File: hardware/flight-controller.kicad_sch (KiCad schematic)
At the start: 10 parts, among them J1 Conn_01x03, J2 Conn_01x03, J3 Conn_01x03, J4 Conn_01x03, J5 Conn_01x02, J6 Conn_01x02, J7 Conn_01x02, J8 Conn_01x02, U1 STM32H723VGTx, U2 LSM6DSOTR

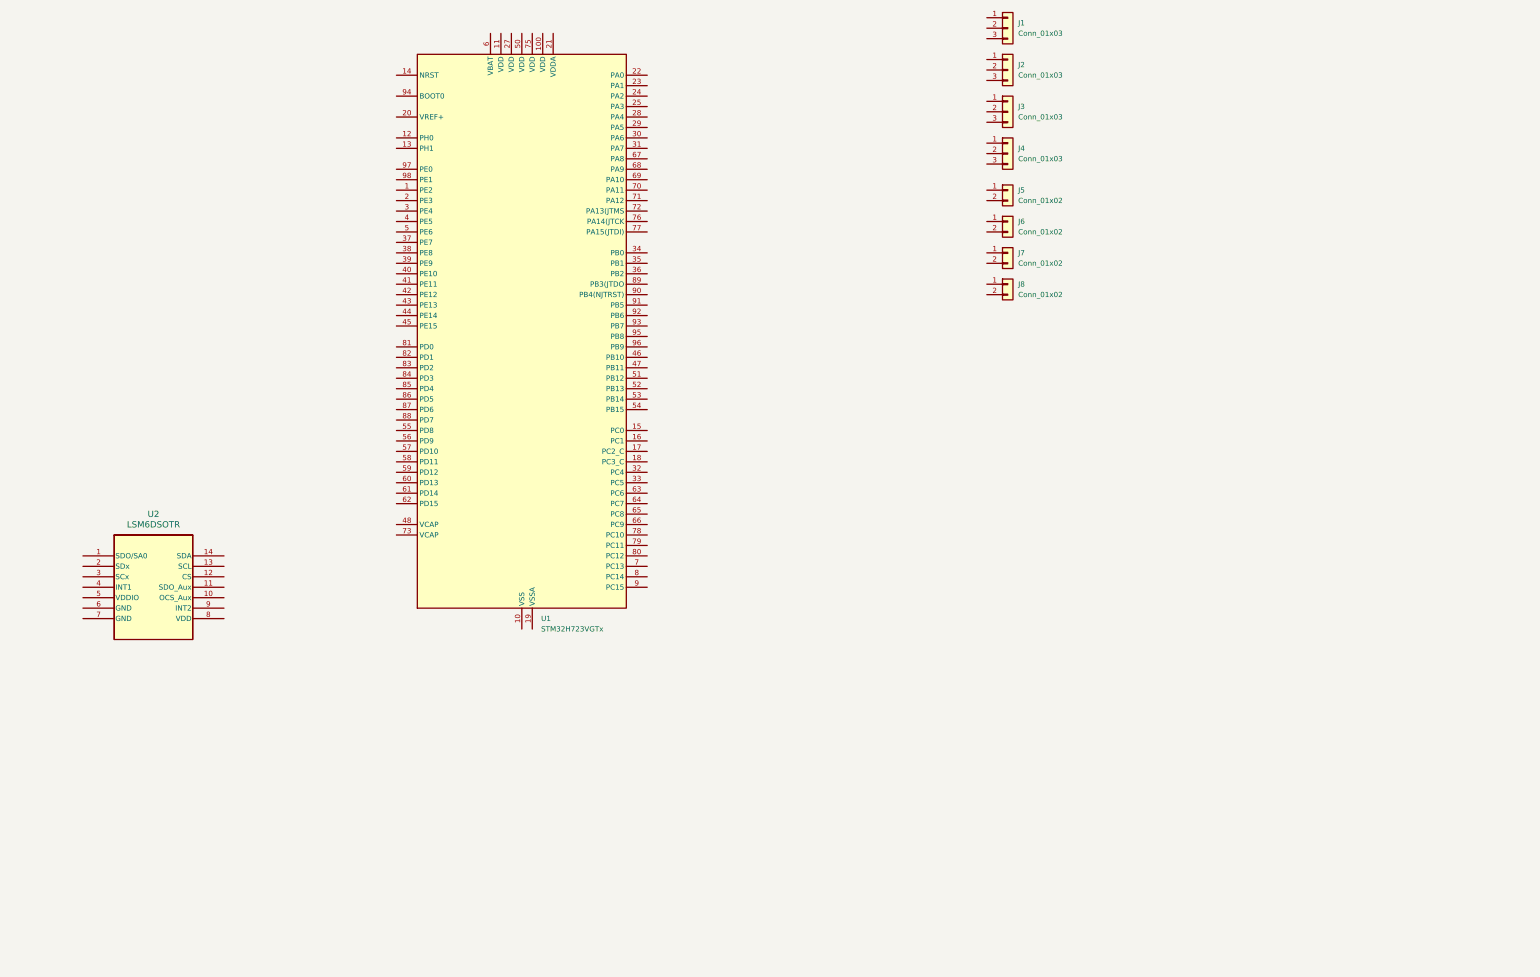
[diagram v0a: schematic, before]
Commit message: made schematic outline
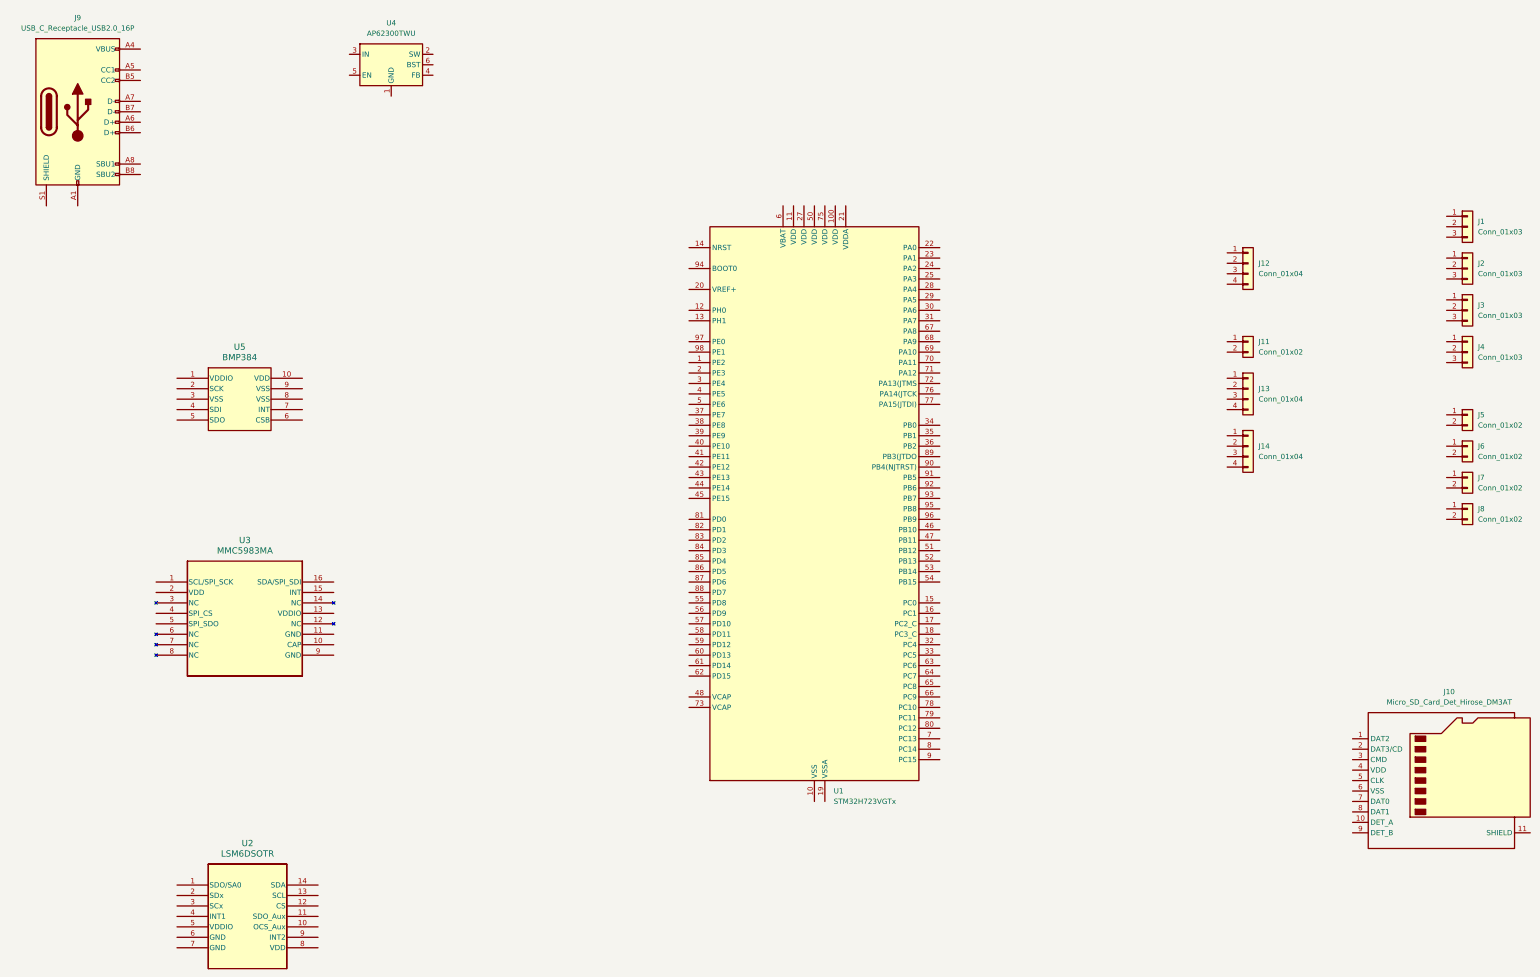
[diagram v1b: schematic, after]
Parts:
- removed U2: LSM6DSOTR, LGA-14L_2P5X3X0P86_STM, symbol Imports:LSM6DSOTR
- added J10: Micro_SD_Card_Det_Hirose_DM3AT, symbol Connector:Micro_SD_Card_Det_Hirose_DM3AT
- added J11: Conn_01x02, symbol Connector_Generic:Conn_01x02
- added J12, J13, J14: Conn_01x04, symbol Connector_Generic:Conn_01x04
- added J9: USB_C_Receptacle_USB2.0_16P, symbol Connector:USB_C_Receptacle_USB2.0_16P
- added U2: LSM6DSOTR, LGA-14L_2P5X3X0P86_STM, symbol Flight-Controller_Imports:LSM6DSOTR
- added U3: MMC5983MA, MMC5983MA_MEM, symbol Flight-Controller_Imports:MMC5983MA
- added U4: AP62300TWU, Package_TO_SOT_SMD:TSOT-23-6, symbol Regulator_Switching:AP62300TWU
- added U5: BMP384, LGA10_2.0X2.0X0.95_BOS, symbol Flight-Controller_Imports:BMP384
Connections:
- new net: J9.A1 (GND), J9.A12 (GND), J9.B1 (GND), J9.B12 (GND)
- new net: J9.A4 (VBUS), J9.A9 (VBUS), J9.B4 (VBUS), J9.B9 (VBUS)
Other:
- moved on the sheet: J1, J2, J3, J4, J5, J6, J7, J8, U1
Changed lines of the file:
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@@
 	(generator "eeschema")
 	(generator_version "9.0")
-	(paper "A4")
+	(paper "A3")

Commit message: added gps
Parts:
- added U6: NEO-M9N, RF_GPS:ublox_NEO, symbol RF_GPS:NEO-M9N
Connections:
- new net: U6.10 (GND), U6.12 (GND), U6.13 (GND), U6.24 (GND)
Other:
- moved on the sheet: J1, J11, J12, J13, J14, J2, J3, J4, J5, J6, J7, J8

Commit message: worked on schematic
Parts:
- added BOOT, RESET: SW_Push, symbol Switch:SW_Push
- added C1, C17, C2, C21, C23, C24, C27, C3, C4, C5, C8, C9: 100nF, Capacitor_SMD:C_0402_1005Metric, symbol Device:C
- added C10: 4.7uF, Capacitor_SMD:C_0402_1005Metric, symbol Device:C
- added C11, C12: 2.2uF, Capacitor_SMD:C_0402_1005Metric, symbol Device:C
- added C13, C14: 27pF, Capacitor_SMD:C_0402_1005Metric, symbol Device:C
- added C15, C16: 15pF, Capacitor_SMD:C_0402_1005Metric, symbol Device:C
- added C18, C25: 10uF, Capacitor_SMD:C_0402_1005Metric, symbol Device:C
- added C19, C20: 22uF, Capacitor_SMD:C_0402_1005Metric, symbol Device:C
- added C22: 10pF, Capacitor_SMD:C_0402_1005Metric, symbol Device:C
- added C26, C6, C7: 1uF, Capacitor_SMD:C_0402_1005Metric, symbol Device:C
- added D1: LED, LED_SMD:LED_0603_1608Metric, symbol Device:LED
- added FB1: FerriteBead, symbol Device:FerriteBead
- added L1: 3.3uH, symbol Device:L
- added R1: 47, symbol Device:R
- added R10, R11, R12, R13, R14, R15, R2, R3, R8: 10K, symbol Device:R
- added R4, R5: 27, symbol Device:R
- added R6, R7: 5.1K, symbol Device:R
- added R9: 33.2K, symbol Device:R
- added Y1: Q13FC13500004, symbol Device:Crystal
- added Y2: X322512MSB4SI, symbol Device:Crystal_GND24
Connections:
- net GND: now reaches U1.10 (VSS), U1.26 (VSS), U1.49 (VSS), U1.74 (VSS), U1.99 (VSS)
- net GND: now also J10.11 (SHIELD), J10.6 (VSS), J9.A1 (GND), J9.A12 (GND), J9.B1 (GND), J9.B12 (GND), J9.S1 (SHIELD), U1.19 (VSSA), U2.2 (SDx), U2.3 (SCx), U2.6 (GND), U2.7 (GND), U3.11 (GND), U3.9 (GND), U4.1 (GND), C1.2, C10.2, C11.2, C12.2, C13.2, C14.2, C15.2, C16.2, C17.1, C18.2, C19.2, C2.2, C20.2, C23.2, C24.2, C25.2, C26.2, C27.2, C3.2, C4.2, C5.2, C6.2, C7.2, C8.2, C9.2, D1.1 (K), R2.2, R6.2, R7.1, R9.2, RESET.1, Y2.2 (G), Y2.4 (G)
- net +3.3V: now reaches U1.100 (VDD)
- net +3.3V: now also J10.4 (VDD), U1.11 (VDD), U1.27 (VDD), U1.50 (VDD), U1.6 (VBAT), U1.75 (VDD), U2.5 (VDDIO), U2.8 (VDD), U3.13 (VDDIO), U3.2 (VDD), U3.4 (SPI_CS), BOOT.1, C1.1, C10.1, C19.1, C2.1, C20.1, C22.1, C23.1, C24.1, C26.1, C27.1, C3.1, C4.1, C5.1, C6.1, C7.1, C8.1, C9.1, FB1.1, L1.2, R1.1, R10.1, R11.1, R12.1, R13.1, R14.1, R15.1, R8.1
- net HSE_IN: now reaches U1.12 (PH0)
- net HSE_IN: now also C13.1, Y2.1
- net HSE_OUT: now reaches U1.13 (PH1)
- net HSE_OUT: now also C14.1, Y2.3
- net RESET: now reaches U1.14 (NRST)
- net RESET: now also C17.2, RESET.2
- net at U1.20 (VREF+): now also R1.2
- net at U1.21 (VDDA): now also FB1.2
- net UART4_TX: now reaches U1.22 (PA0)
- net UART4_RX: now reaches U1.23 (PA1)
- net UART2_TX: now reaches U1.24 (PA2)
- net UART2_RX: now reaches U1.25 (PA3)
- net SPI_NSS: now reaches U1.28 (PA4)
- net SPI_NSS: now also U2.12 (CS)
- net SPI_SCK: now reaches U1.29 (PA5)
- net SPI_SCK: now also U2.13 (SCL)
- net SPI_MISO: now reaches U1.30 (PA6)
- net SPI_MISO: now also U2.1 (SDO/SA0)
- net SPI_MOSI: now reaches U1.31 (PA7)
- net SPI_MOSI: now also U2.14 (SDA)
- net LSM_INT: now reaches U1.32 (PC4)
- net LSM_INT: now also U2.4 (INT1)
- net BAT_ADC: now reaches U1.34 (PB0)
- net UART3_TX: now reaches U1.46 (PB10)
- net UART3_RX: now reaches U1.47 (PB11)
- net at U1.48 (VCAP): now also C12.1
- net GPS_INT: now reaches U1.52 (PB13)
- net GPS_TX: now reaches U1.53 (PB14)
- net GPS_RX: now reaches U1.54 (PB15)
- net PWM_1: now reaches U1.59 (PD12)
- net PWM_2: now reaches U1.60 (PD13)
- net PWM_3: now reaches U1.61 (PD14)
- net PWM_4: now reaches U1.62 (PD15)
- net SD_D0: now reaches U1.65 (PC8)
- net SD_D0: now also J10.7 (DAT0), R11.2
- net SD_D1: now reaches U1.66 (PC9)
- net SD_D1: now also J10.8 (DAT1), R10.2
- net at U1.70 (PA11): now also R4.1
- net at U1.71 (PA12): now also R5.2
- net SWDIO: now reaches U1.72 (PA13(JTMS)
- net at U1.73 (VCAP): now also C11.1
- net SWDCLK: now reaches U1.76 (PA14(JTCK)
- net SD_D2: now reaches U1.78 (PC10)
- net SD_D2: now also J10.1 (DAT2), R15.2
- net SD_D3: now reaches U1.79 (PC11)
- net SD_D3: now also J10.2 (DAT3/CD), R14.2
- net LSE_IN: now reaches U1.8 (PC14)
- net LSE_IN: now also C15.1, Y1.1
- net SD_CLK: now reaches U1.80 (PC12)
- net SD_CLK: now also J10.5 (CLK), R12.2
- net SD_CMD: now reaches U1.83 (PD2)
- net SD_CMD: now also J10.3 (CMD), R13.2
- net SD_DET1: now reaches U1.84 (PD3)
- net SD_DET1: now also J10.10 (DET_A)
- net SD_DET2: now reaches U1.85 (PD4)
- net SD_DET2: now also J10.9 (DET_B)
- net LSE_OUT: now reaches U1.9 (PC15)
- net LSE_OUT: now also C16.1, Y1.2
- net BMP_INT: now reaches U1.90 (PB4(NJTRST))
- net MMC_INT: now reaches U1.91 (PB5)
- net MMC_INT: now also U3.15 (INT)
- net SCL: now reaches U1.92 (PB6)
- net SCL: now also U3.1 (SCL/SPI_SCK)
- net SDA: now reaches U1.93 (PB7)
- net SDA: now also U3.16 (SDA/SPI_SDI)
- net BOOT: now reaches U1.94 (BOOT0)
- net BOOT: now also BOOT.2, R2.1
- net at U1.97 (PE0): now also R3.1
- net at U3.10 (CAP): now also C25.1
- net VBUS: now reaches J9.A4 (VBUS), J9.A9 (VBUS), J9.B4 (VBUS), J9.B9 (VBUS)
- net VBUS: now also U4.3 (IN), U4.5 (EN), C18.1
- net at J9.A5 (CC1): now also R6.1
- net USB_-: now reaches J9.A6 (D+)
- net USB_-: now also J9.B6 (D+), R4.2
- net USB_+: now reaches J9.A7 (D-)
- net USB_+: now also J9.B7 (D-), R5.1
- net at J9.B5 (CC2): now also R7.2
- net at U4.2 (SW): now also C21.1, L1.1
- net at U4.4 (FB): now also C22.2, R8.2, R9.1
- net at U4.6 (BST): now also C21.2
- new net: D1.2 (A), R3.2
- no-connect marks 0 -> 6
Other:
- moved on the sheet: J10, J9, U1, U2, U3, U4, U5

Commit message: routed schematic
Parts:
- removed J12: Conn_01x04, symbol Connector_Generic:Conn_01x04
- added BT1: Battery, symbol Device:Battery_Cell
- added C28, C29: 100nF, Capacitor_SMD:C_0402_1005Metric, symbol Device:C
- added C30, C35: 1uF, Capacitor_SMD:C_0402_1005Metric, symbol Device:C
- added C31, C32, C33, C34, C36, C37: 10uF, Capacitor_SMD:C_0402_1005Metric, symbol Device:C
- added D2, D3: LED, LED_SMD:LED_0603_1608Metric, symbol Device:LED
- added D4: D_Schottky, symbol Device:D_Schottky
- added J12, J16: Conn_01x02, symbol Connector_Generic:Conn_01x02
- added J15: Conn_Coaxial, Connector_Coaxial:U.FL_Molex_MCRF_73412-0110_Vertical, symbol Connector:Conn_Coaxial
- added J17: Conn_01x04, symbol Connector_Generic:Conn_01x04
- added R16, R17, R18: 1K, symbol Device:R
- added R19: 3K, symbol Device:R
- added R20, R22, R24, R26: 5K, symbol Device:R
- added R21: 23.7, symbol Device:R
- added R23: 60K, symbol Device:R
- added R25, R27: 30K, symbol Device:R
- added TP1: TestPoint, Connector_Pin:Pin_D1.0mm_L10.0mm_LooseFit, symbol Connector:TestPoint
- added U7: TPS2121RUXR, TPS2121RUXR:IC_TPS2121RUXR, symbol Flight-Controller_Imports:TPS2121RUXR
- R3: value 10K -> 1K
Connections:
- net +3.3V: now also J13.1 (Pin_1), J14.1 (Pin_1), U5.1 (VDDIO), U5.10 (VDD), U6.23 (VCC), C28.1, C29.1, C37.1, D4.2 (A), J12.1 (Pin_1), J17.1 (Pin_1), R17.1
- net BMP_INT: now also U5.7 (INT)
- net GND: now also J1.3 (Pin_3), J11.2 (Pin_2), J13.2 (Pin_2), J14.2 (Pin_2), J2.3 (Pin_3), J3.3 (Pin_3), J4.3 (Pin_3), J5.2 (Pin_2), J6.2 (Pin_2), J7.2 (Pin_2), J8.2 (Pin_2), U5.3 (VSS), U5.5 (SDO), U5.8 (VSS), U5.9 (VSS), U6.10 (GND), U6.12 (GND), U6.13 (GND), U6.24 (GND), U6.7 (VDD_USB), BT1.2 (-), C28.2, C29.2, C30.2, C31.2, C32.2, C33.2, C34.2, C35.2, C36.2, C37.2, D2.1 (K), D3.1 (K), J12.2 (Pin_2), J15.2 (Ext), J16.2 (Pin_2), J17.2 (Pin_2), R20.2, R22.2, R24.2, R26.2, R27.2, U7.12 (GND), U7.9 (ST)
- net GPS_INT: now also U6.4 (EXTINT)
- net GPS_RX: now also U6.20 (TXD/SPI_MISO)
- net GPS_TX: now also U6.21 (RXD/SPI_MOSI)
- net PWM_1: now also J1.1 (Pin_1)
- net PWM_2: now also J2.1 (Pin_1)
- net PWM_3: now also J3.1 (Pin_1)
- net PWM_4: now also J4.1 (Pin_1)
- net SCL: now also U5.2 (SCK)
- net SDA: now also U5.4 (SDI)
- net UART2_RX: now also J13.4 (Pin_4)
- net UART2_TX: now also J13.3 (Pin_3)
- net UART3_RX: now also J17.4 (Pin_4)
- net UART3_TX: now also J17.3 (Pin_3)
- net UART4_RX: now also J14.4 (Pin_4)
- net UART4_TX: now also J14.3 (Pin_3)
- net VBUS: now also R19.1, R21.1, U7.7 (IN1); no longer C18.1, U4.3 (IN), U4.5 (EN)
- net LSM_INT2: now reaches U1.33 (PC5)
- net LSM_INT2: now also U2.9 (INT2)
- net GPS_RESET: now reaches U1.51 (PB12)
- net GPS_RESET: now also U6.8 (~{RESET})
- net STAT_LED: now reaches R3.1, U1.97 (PE0)
- net +BATT: now reaches J11.1 (Pin_1)
- net +BATT: now also J5.1 (Pin_1), J6.1 (Pin_1), J7.1 (Pin_1), J8.1 (Pin_1), C31.1, C32.1, C33.1, C34.1, C36.1, J16.1 (Pin_1), R23.1, R25.1, U7.2 (IN2)
- net at U6.1 (~{SAFEBOOT}): now also TP1.1
- net at U6.11 (RF_IN): now also J15.1 (In)
- net V_BCKP: now reaches U6.22 (V_BCKP)
- net V_BCKP: now also BT1.1 (+), C30.1, R18.2
- net GPS_LED: now reaches U6.3 (TIMEPULSE)
- net GPS_LED: now also R16.1
- net LSM_INT renamed LSM_INT1
- new net: R23.2, R24.1, U7.4 (OV2)
- new net: D2.2 (A), R16.2
- new net: R21.2, R22.1, U7.5 (OV1)
- new net: R25.2, R26.1, U7.3 (CP2)
- new net: R27.1, U7.10 (ILIM)
- new net: C35.1, U7.11 (SS)
- new net: R19.2, R20.1, U7.6 (PR1)
- new net: D4.1 (K), R18.1
- new net: D3.2 (A), R17.2
- new net VDD: C18.1, U4.3 (IN), U4.5 (EN), U7.1 (OUT), U7.8 (OUT__2)
- no-connect marks 6 -> 17
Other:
- moved on the sheet: BOOT, C1, C10, C11, C12, C13, C14, C15, C16, C17, C18, C19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

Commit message: worked on layout
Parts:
- removed J11, J12, J5, J6, J7, J8: Conn_01x02, symbol Connector_Generic:Conn_01x02
- added C38: 22uF, Capacitor_SMD:C_1206_3216Metric, symbol Device:C
- added J10, J16, J18, J5, J7, J9: Screw_Terminal_01x02, TerminalBlock_4Ucon:TerminalBlock_4Ucon_1x02_P3.50mm_Horizontal, symbol Connector:Screw_Terminal_01x02
- BOOT1: renamed from BOOT; footprint (none) -> Button_Switch_SMD:SW_Push_SPST_NO_Alps_SKRK
- BT1: value Battery -> MS621FE-FL11E; footprint (none) -> Flight-Controller_Imports:BAT_MS621FE-FL11E
- C1: renamed from C26; footprint Capacitor_SMD:C_0402_1005Metric -> Capacitor_SMD:C_0603_1608Metric
- C14: value 27pF -> 18pF
- C16: renamed from C18; footprint Capacitor_SMD:C_0402_1005Metric -> Capacitor_SMD:C_0603_1608Metric
- C19: renamed from C6; footprint Capacitor_SMD:C_0402_1005Metric -> Capacitor_SMD:C_0603_1608Metric
- C21: renamed from C7; footprint Capacitor_SMD:C_0402_1005Metric -> Capacitor_SMD:C_0603_1608Metric
- C26: renamed from C19; footprint Capacitor_SMD:C_0402_1005Metric -> Capacitor_SMD:C_0603_1608Metric
- C28: renamed from C20; footprint Capacitor_SMD:C_0402_1005Metric -> Capacitor_SMD:C_0603_1608Metric
- C31: renamed from C10; footprint Capacitor_SMD:C_0402_1005Metric -> Capacitor_SMD:C_0603_1608Metric
- C32: renamed from C36; footprint Capacitor_SMD:C_0402_1005Metric -> Capacitor_SMD:C_0805_2012Metric
- C33: renamed from C37; footprint Capacitor_SMD:C_0402_1005Metric -> Capacitor_SMD:C_0805_2012Metric
- C34: renamed from C31; footprint Capacitor_SMD:C_0402_1005Metric -> Capacitor_SMD:C_0805_2012Metric
- C35: renamed from C33; footprint Capacitor_SMD:C_0402_1005Metric -> Capacitor_SMD:C_0805_2012Metric
- C36: renamed from C32; footprint Capacitor_SMD:C_0402_1005Metric -> Capacitor_SMD:C_0805_2012Metric
- C37: renamed from C34; footprint Capacitor_SMD:C_0402_1005Metric -> Capacitor_SMD:C_0805_2012Metric
- C5: renamed from C25; footprint Capacitor_SMD:C_0402_1005Metric -> Capacitor_SMD:C_0603_1608Metric
- C8: renamed from C30; footprint Capacitor_SMD:C_0402_1005Metric -> Capacitor_SMD:C_0603_1608Metric
- C9: renamed from C13; value 27pF -> 18pF
- D1: renamed from D4; footprint (none) -> Diode_SMD:D_0603_1608Metric
- FB1: footprint (none) -> Inductor_SMD:L_0603_1608Metric
- J1: renamed from J9; footprint (none) -> Connector_USB:USB_C_Receptacle_GCT_USB4105-xx-A_16P_TopMnt_Horizontal
- J11: renamed from J10; footprint (none) -> Connector_Card:microSD_HC_Hirose_DM3AT-SF-PEJM5
- J12: renamed from J1; footprint (none) -> Connector_PinHeader_2.54mm:PinHeader_1x03_P2.54mm_Vertical
- J13: renamed from J2; footprint (none) -> Connector_PinHeader_2.54mm:PinHeader_1x03_P2.54mm_Vertical
- J14: renamed from J3; footprint (none) -> Connector_PinHeader_2.54mm:PinHeader_1x03_P2.54mm_Vertical
- J15: renamed from J4; footprint (none) -> Connector_PinHeader_2.54mm:PinHeader_1x03_P2.54mm_Vertical
- J2: renamed from J16; footprint (none) -> Connector_AMASS:AMASS_XT60-M_1x02_P7.20mm_Vertical
- J4: renamed from J13; footprint (none) -> Connector_JST:JST_XH_B4B-XH-A_1x04_P2.50mm_Vertical
- J6: renamed from J17; footprint (none) -> Connector_JST:JST_XH_B4B-XH-A_1x04_P2.50mm_Vertical
- J8: renamed from J14; footprint (none) -> Connector_JST:JST_XH_B4B-XH-A_1x04_P2.50mm_Vertical
- L1: footprint (none) -> Flight-Controller_Imports:IND_SRP4030FA_BRN
- R1: renamed from R6; footprint (none) -> Resistor_SMD:R_0402_1005Metric
- R10: renamed from R25; footprint (none) -> Resistor_SMD:R_0402_1005Metric
- R11: renamed from R26; footprint (none) -> Resistor_SMD:R_0402_1005Metric
- R12: renamed from R27; value 30K -> 50K; footprint (none) -> Resistor_SMD:R_0603_1608Metric
- R13: renamed from R3; footprint (none) -> Resistor_SMD:R_0402_1005Metric
- R14: renamed from R16; footprint (none) -> Resistor_SMD:R_0402_1005Metric
- R15: renamed from R17; footprint (none) -> Resistor_SMD:R_0402_1005Metric
- R16: renamed from R2; footprint (none) -> Resistor_SMD:R_0402_1005Metric
- R17: renamed from R1; footprint (none) -> Resistor_SMD:R_0402_1005Metric
- R18: renamed from R8; footprint (none) -> Resistor_SMD:R_0402_1005Metric
- R19: renamed from R9; footprint (none) -> Resistor_SMD:R_0402_1005Metric
- R2: renamed from R7; footprint (none) -> Resistor_SMD:R_0402_1005Metric
- R20: renamed from R4; footprint (none) -> Resistor_SMD:R_0402_1005Metric
- R21: renamed from R5; footprint (none) -> Resistor_SMD:R_0402_1005Metric
- R22: renamed from R15; footprint (none) -> Resistor_SMD:R_0402_1005Metric
- R23: renamed from R14; footprint (none) -> Resistor_SMD:R_0402_1005Metric
- R24: renamed from R13; footprint (none) -> Resistor_SMD:R_0402_1005Metric
- R25: renamed from R12; footprint (none) -> Resistor_SMD:R_0402_1005Metric
- R26: renamed from R11; footprint (none) -> Resistor_SMD:R_0402_1005Metric
- R27: renamed from R10; footprint (none) -> Resistor_SMD:R_0402_1005Metric
- R3: renamed from R18; footprint (none) -> Resistor_SMD:R_0402_1005Metric
- R4: renamed from R21; value 23.7 -> 23.7K; footprint (none) -> Resistor_SMD:R_0402_1005Metric
- R5: renamed from R22; footprint (none) -> Resistor_SMD:R_0402_1005Metric
- R6: renamed from R23; footprint (none) -> Resistor_SMD:R_0402_1005Metric
- R7: renamed from R24; footprint (none) -> Resistor_SMD:R_0402_1005Metric
- R8: renamed from R19; value 3K -> 4K; footprint (none) -> Resistor_SMD:R_0402_1005Metric
- R9: renamed from R20; footprint (none) -> Resistor_SMD:R_0402_1005Metric
- RESET1: renamed from RESET; footprint (none) -> Button_Switch_SMD:SW_Push_SPST_NO_Alps_SKRK
- TP1: footprint Connector_Pin:Pin_D1.0mm_L10.0mm_LooseFit -> TestPoint:TestPoint_Pad_D1.0mm
- U1: renamed from U5; footprint LGA10_2.0X2.0X0.95_BOS -> Package_LGA:Rohm_MLGA010V020A_LGA-10_2x2mm_P0.45mm_LayoutBorder2x3y
- U2: footprint LGA-14L_2P5X3X0P86_STM -> Package_LGA:LGA-14_3x2.5mm_P0.5mm_LayoutBorder3x4y
- U3: footprint MMC5983MA_MEM -> Package_LGA:LGA-16_3x3mm_P0.5mm
- U5: renamed from U7; footprint TPS2121RUXR:IC_TPS2121RUXR -> Flight-Controller_Imports:IC_TPS2121RUXR
- Y1: footprint (none) -> Crystal:Crystal_SMD_3215-2Pin_3.2x1.5mm
- Y2: value X322512MSB4SI -> X322525MOB4SI; footprint (none) -> Crystal:Crystal_SMD_3225-4Pin_3.2x2.5mm; private KLC_S4.1 -> (none)
- renumbered C15 to C10, C17 to C11, C35 to C12, C16 to C13, C12 to C15, C11 to C17, C9 to C18, C24 to C2, C8 to C20, C21 to C22, C22 to C23, C1 to C24, C2 to C25, C3 to C27, C4 to C29, C23 to C3, C5 to C30, C28 to C4, C29 to C6, C27 to C7, D1 to D2, D2 to D3, D3 to D4, J15 to J3, U6 to U4, U4 to U6, U1 to U7
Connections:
- net +3.3V: now also J5.1 (Pin_1)
- net +BATT: now also C38.1, J10.1 (Pin_1), J16.1 (Pin_1), J18.1 (Pin_1), J7.1 (Pin_1), J9.1 (Pin_1)
- net GND: now also C38.2, J10.2 (Pin_2), J16.2 (Pin_2), J18.2 (Pin_2), J5.2 (Pin_2), J7.2 (Pin_2), J9.2 (Pin_2)
- no-connect marks 17 -> 57
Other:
- moved on the sheet: BT1, C1, C12, C2, C3, C4, C5, C6, C7, C8, D1, J2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

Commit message: added uart port and buzzer
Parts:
- added BZ1: Buzzer, Buzzer_Beeper:Buzzer_12x9.5RM7.6, symbol Device:Buzzer
- added J17: Conn_01x04, Connector_JST:JST_XH_B4B-XH-A_1x04_P2.50mm_Vertical, symbol Connector_Generic:Conn_01x04
- added R28: 100, Resistor_SMD:R_0402_1005Metric, symbol Device:R
- added R29: 13.2K, Resistor_SMD:R_0603_1608Metric, symbol Device:R
- added R30: 5K, Resistor_SMD:R_0402_1005Metric, symbol Device:R
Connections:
- net +3.3V: now also J17.1 (Pin_1)
- net +BATT: now also R29.1
- net BAT_ADC: now also R29.2, R30.1
- net GND: now also BZ1.2 (-), J17.2 (Pin_2), R30.2
- net UART7_RX: now reaches U7.37 (PE7)
- net UART7_RX: now also J17.4 (Pin_4)
- net UART7_TX: now reaches U7.38 (PE8)
- net UART7_TX: now also J17.3 (Pin_3)
- new net: BZ1.1 (+), R28.2
- new net BUZZER: R28.1
- no-connect marks 57 -> 55
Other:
- moved on the sheet: BOOT1, BT1, C11, C12, C15, C17, C18, C19, C20, C21, C24, C25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
